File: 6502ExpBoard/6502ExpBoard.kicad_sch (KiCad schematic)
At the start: 5 parts, among them J1 Expansion / Diag Port, U1 74LS373, U2 74LS373, U3 74LS373, U4 74LS373

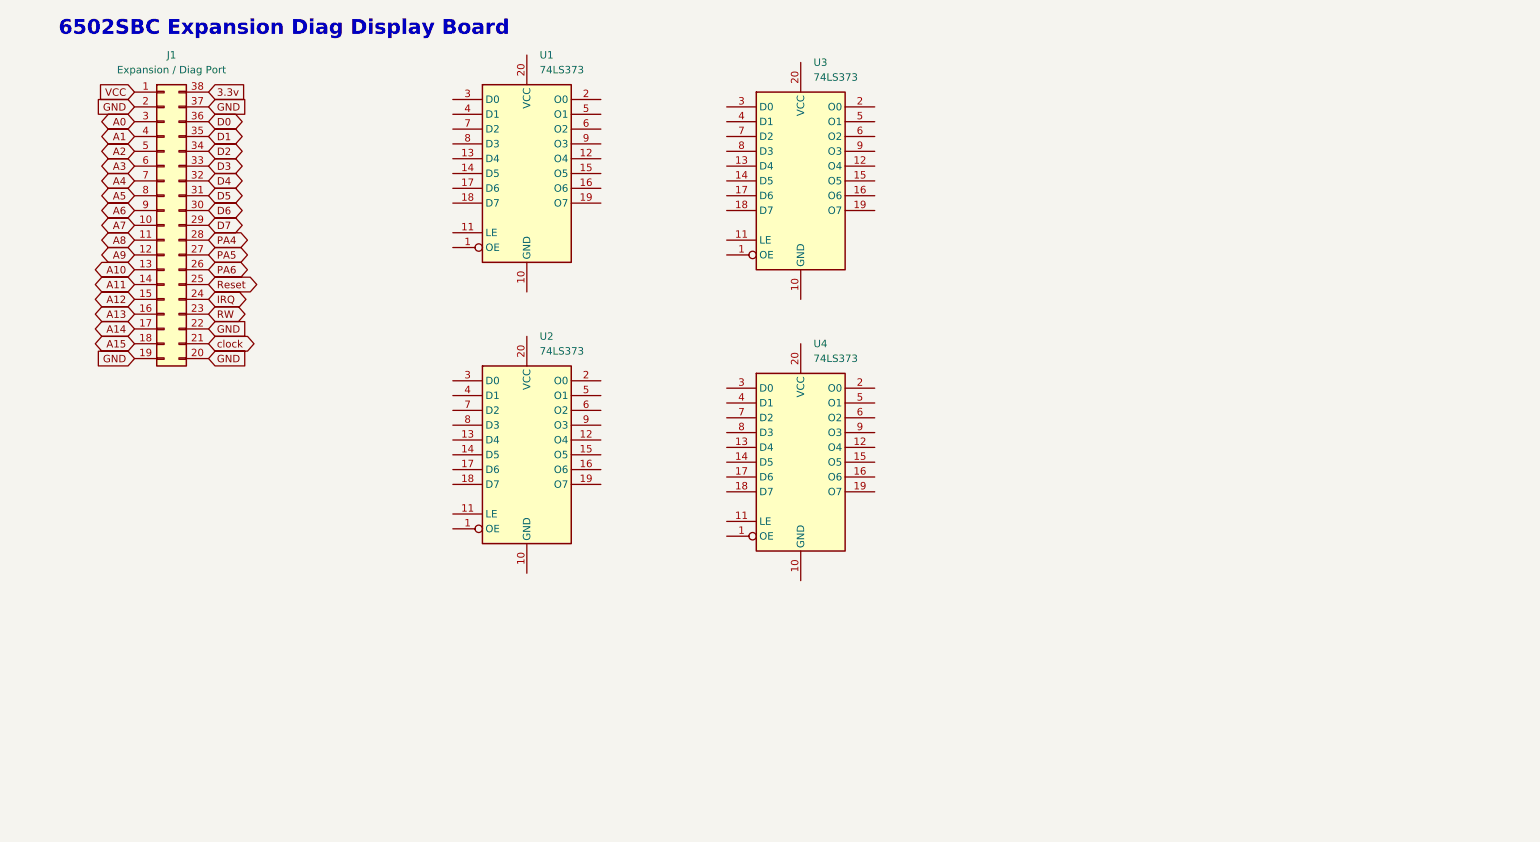
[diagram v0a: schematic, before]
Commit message: Added Expansion
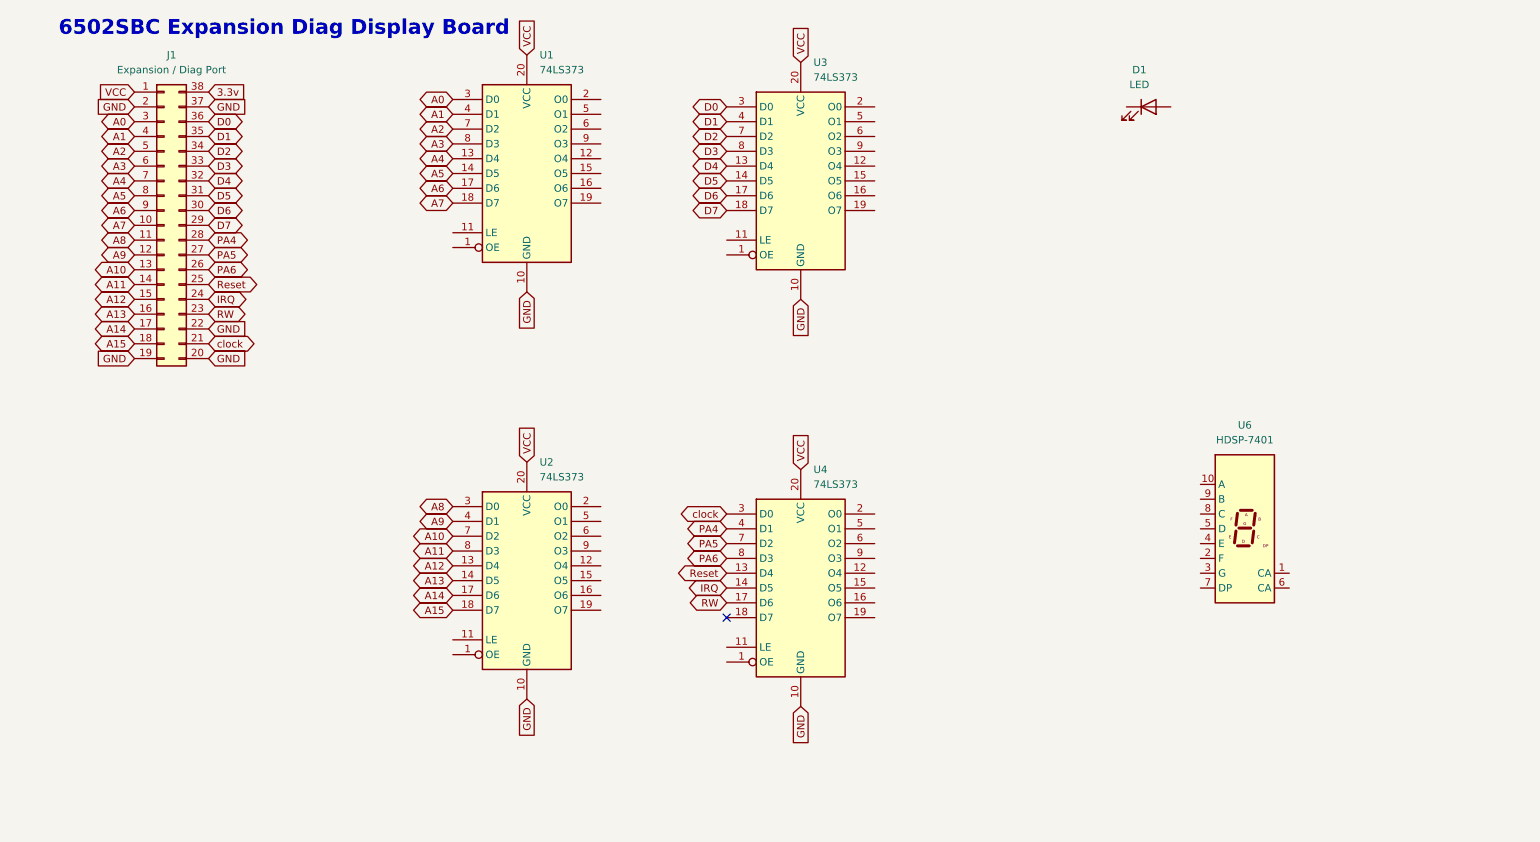
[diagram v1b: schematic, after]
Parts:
- added D1: LED, symbol Device:LED
- added U6: HDSP-7401, Display_7Segment:HDSP-7401, symbol Display_Character:HDSP-7401
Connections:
- net A0: now also U1.3 (D0)
- net A1: now also U1.4 (D1)
- net A10: now also U2.7 (D2)
- net A11: now also U2.8 (D3)
- net A12: now also U2.13 (D4)
- net A13: now also U2.14 (D5)
- net A14: now also U2.17 (D6)
- net A15: now also U2.18 (D7)
- net A2: now also U1.7 (D2)
- net A3: now also U1.8 (D3)
- net A4: now also U1.13 (D4)
- net A5: now also U1.14 (D5)
- net A6: now also U1.17 (D6)
- net A7: now also U1.18 (D7)
- net A8: now also U2.3 (D0)
- net A9: now also U2.4 (D1)
- net D0: now also U3.3 (D0)
- net D1: now also U3.4 (D1)
- net D2: now also U3.7 (D2)
- net D3: now also U3.8 (D3)
- net D4: now also U3.13 (D4)
- net D5: now also U3.14 (D5)
- net D6: now also U3.17 (D6)
- net D7: now also U3.18 (D7)
- net GND: now also U1.10 (GND), U2.10 (GND), U3.10 (GND), U4.10 (GND)
- net IRQ: now also U4.14 (D5)
- net PA4: now also U4.4 (D1)
- net PA5: now also U4.7 (D2)
- net PA6: now also U4.8 (D3)
- net RW: now also U4.17 (D6)
- net Reset: now also U4.13 (D4)
- net VCC: now also U1.20 (VCC), U2.20 (VCC), U3.20 (VCC), U4.20 (VCC)
- net clock: now also U4.3 (D0)
- no-connect marks 0 -> 1
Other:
- moved on the sheet: U2, U4

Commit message: Added Expansion
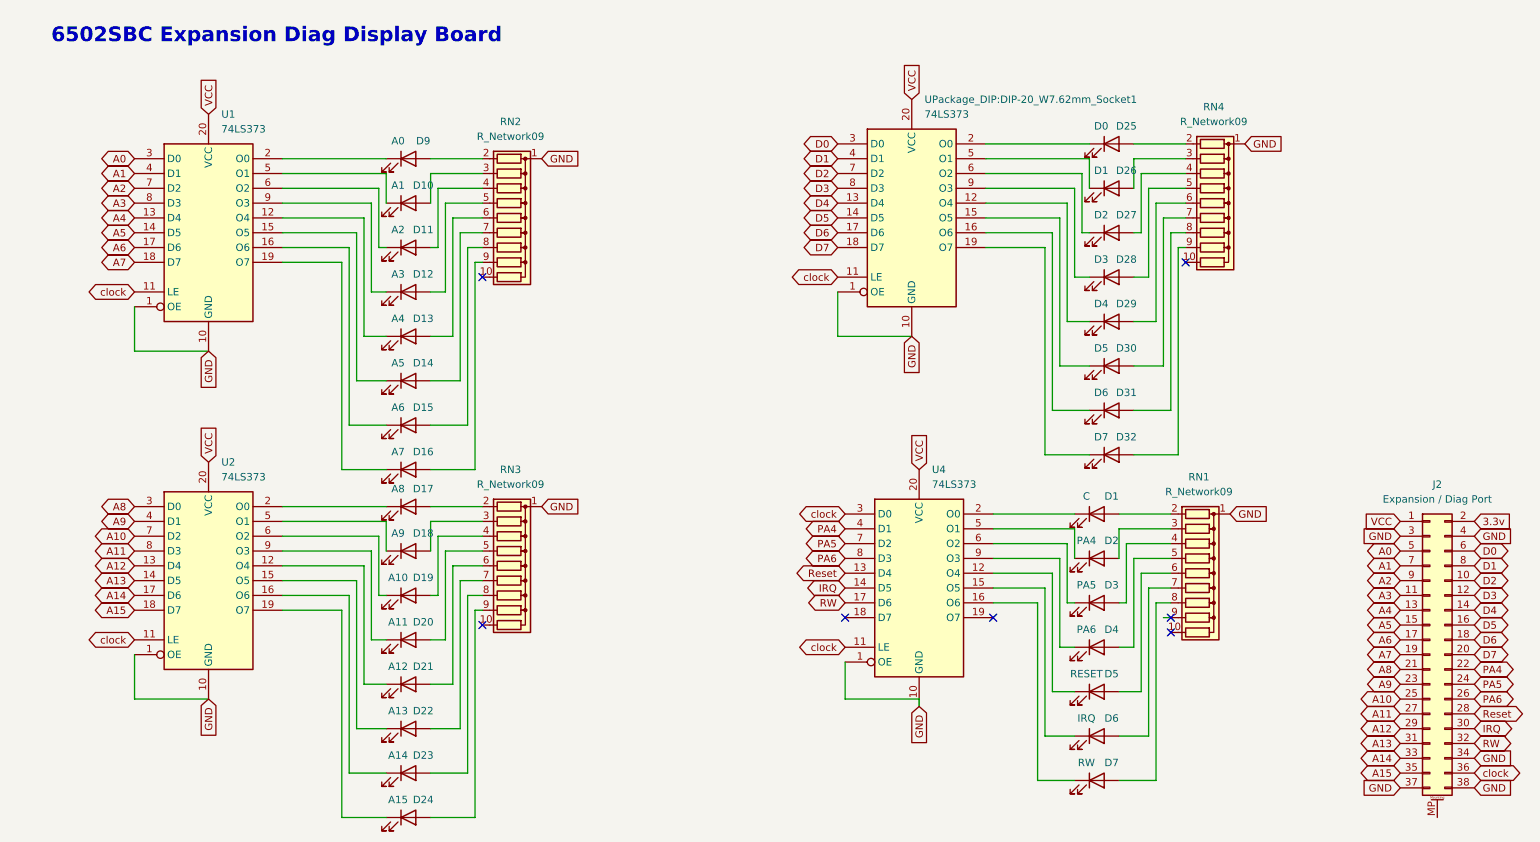
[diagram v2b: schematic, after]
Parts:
- removed J1: Expansion / Diag Port, Connector_PinHeader_2.54mm:PinHeader_1x38_P2.54mm_Horizontal, symbol Connector_Generic:Conn_02x19_Counter_Clockwise
- removed U6: HDSP-7401, Display_7Segment:HDSP-7401, symbol Display_Character:HDSP-7401
- added D10: A1, LED_THT:LED_D3.0mm, symbol Device:LED
- added D11: A2, LED_THT:LED_D3.0mm, symbol Device:LED
- added D12: A3, LED_THT:LED_D3.0mm, symbol Device:LED
- added D13: A4, LED_THT:LED_D3.0mm, symbol Device:LED
- added D14: A5, LED_THT:LED_D3.0mm, symbol Device:LED
- added D15: A6, LED_THT:LED_D3.0mm, symbol Device:LED
- added D16: A7, LED_THT:LED_D3.0mm, symbol Device:LED
- added D17: A8, LED_THT:LED_D3.0mm, symbol Device:LED
- added D18: A9, LED_THT:LED_D3.0mm, symbol Device:LED
- added D19: A10, LED_THT:LED_D3.0mm, symbol Device:LED
- added D2: PA4, LED_THT:LED_D3.0mm, symbol Device:LED
- added D20: A11, LED_THT:LED_D3.0mm, symbol Device:LED
- added D21: A12, LED_THT:LED_D3.0mm, symbol Device:LED
- added D22: A13, LED_THT:LED_D3.0mm, symbol Device:LED
- added D23: A14, LED_THT:LED_D3.0mm, symbol Device:LED
- added D24: A15, LED_THT:LED_D3.0mm, symbol Device:LED
- added D25: D0, LED_THT:LED_D3.0mm, symbol Device:LED
- added D26: D1, LED_THT:LED_D3.0mm, symbol Device:LED
- added D27: D2, LED_THT:LED_D3.0mm, symbol Device:LED
- added D28: D3, LED_THT:LED_D3.0mm, symbol Device:LED
- added D29: D4, LED_THT:LED_D3.0mm, symbol Device:LED
- added D3: PA5, LED_THT:LED_D3.0mm, symbol Device:LED
- added D30: D5, LED_THT:LED_D3.0mm, symbol Device:LED
- added D31: D6, LED_THT:LED_D3.0mm, symbol Device:LED
- added D32: D7, LED_THT:LED_D3.0mm, symbol Device:LED
- added D4: PA6, LED_THT:LED_D3.0mm, symbol Device:LED
- added D5: RESET, LED_THT:LED_D3.0mm, symbol Device:LED
- added D6: IRQ, LED_THT:LED_D3.0mm, symbol Device:LED
- added D7: RW, LED_THT:LED_D3.0mm, symbol Device:LED
- added D9: A0, LED_THT:LED_D3.0mm, symbol Device:LED
- added J2: Expansion / Diag Port, Connector_PinHeader_2.54mm:PinHeader_2x19_P2.54mm_Vertical, symbol Connector_Generic_MountingPin:Conn_02x19_Odd_Even_MountingPin
- added RN1, RN2, RN3, RN4: R_Network09, Resistor_THT:R_Array_SIP10, symbol Device:R_Network09
- D1: value LED -> C; footprint (none) -> LED_THT:LED_D3.0mm
- U1, U2, U4: footprint (none) -> Package_DIP:DIP-20_W7.62mm_Socket
- UPackage_DIP:DIP-20_W7.62mm_Socket1: renamed from U3; footprint (none) -> Package_DIP:DIP-20_W7.62mm_Socket
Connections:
- net 3.3v: now also J2.2 (Pin_2)
- net A0: now also J2.5 (Pin_5)
- net A1: now also J2.7 (Pin_7)
- net A10: now also J2.25 (Pin_25)
- net A11: now also J2.27 (Pin_27)
- net A12: now also J2.29 (Pin_29)
- net A13: now also J2.31 (Pin_31)
- net A14: now also J2.33 (Pin_33)
- net A15: now also J2.35 (Pin_35)
- net A2: now also J2.9 (Pin_9)
- net A3: now also J2.11 (Pin_11)
- net A4: now also J2.13 (Pin_13)
- net A5: now also J2.15 (Pin_15)
- net A6: now also J2.17 (Pin_17)
- net A7: now also J2.19 (Pin_19)
- net A8: now also J2.21 (Pin_21)
- net A9: now also J2.23 (Pin_23)
- net D0: now also J2.6 (Pin_6)
- net D1: now also J2.8 (Pin_8)
- net D2: now also J2.10 (Pin_10)
- net D3: now also J2.12 (Pin_12)
- net D4: now also J2.14 (Pin_14)
- net D5: now also J2.16 (Pin_16)
- net D6: now also J2.18 (Pin_18)
- net D7: now also J2.20 (Pin_20)
- net GND: now also U1.1 (OE), U2.1 (OE), U4.1 (OE), UPackage_DIP:DIP-20_W7.62mm_Socket1.1 (OE), J2.3 (Pin_3), J2.34 (Pin_34), J2.37 (Pin_37), J2.38 (Pin_38), J2.4 (Pin_4), RN1.1 (common), RN2.1 (common), RN3.1 (common), RN4.1 (common)
- net IRQ: now also J2.30 (Pin_30)
- net PA4: now also J2.22 (Pin_22)
- net PA5: now also J2.24 (Pin_24)
- net PA6: now also J2.26 (Pin_26)
- net RW: now also J2.32 (Pin_32)
- net Reset: now also J2.28 (Pin_28)
- net VCC: now also J2.1 (Pin_1)
- net clock: now also U1.11 (LE), U2.11 (LE), U4.11 (LE), UPackage_DIP:DIP-20_W7.62mm_Socket1.11 (LE), J2.36 (Pin_36)
- net at U4.12 (O4): now also D5.1 (K)
- net at U4.15 (O5): now also D6.1 (K)
- net at U4.16 (O6): now also D7.1 (K)
- net at U4.2 (O0): now also D1.1 (K)
- net at U4.5 (O1): now also D2.1 (K)
- net at U4.6 (O2): now also D3.1 (K)
- net at U4.9 (O3): now also D4.1 (K)
- net at D1.2 (A): now also RN1.2 (R1)
- net at UPackage_DIP:DIP-20_W7.62mm_Socket1.12 (O4): now also D29.1 (K)
- net at UPackage_DIP:DIP-20_W7.62mm_Socket1.15 (O5): now also D30.1 (K)
- net at UPackage_DIP:DIP-20_W7.62mm_Socket1.16 (O6): now also D31.1 (K)
- net at UPackage_DIP:DIP-20_W7.62mm_Socket1.19 (O7): now also D32.1 (K)
- net at UPackage_DIP:DIP-20_W7.62mm_Socket1.2 (O0): now also D25.1 (K)
- net at UPackage_DIP:DIP-20_W7.62mm_Socket1.5 (O1): now also D26.1 (K)
- net at UPackage_DIP:DIP-20_W7.62mm_Socket1.6 (O2): now also D27.1 (K)
- net at UPackage_DIP:DIP-20_W7.62mm_Socket1.9 (O3): now also D28.1 (K)
- net at U1.12 (O4): now also D13.1 (K)
- net at U1.15 (O5): now also D14.1 (K)
- net at U1.16 (O6): now also D15.1 (K)
- net at U1.19 (O7): now also D16.1 (K)
- net at U1.2 (O0): now also D9.1 (K)
- net at U1.5 (O1): now also D10.1 (K)
- net at U1.6 (O2): now also D11.1 (K)
- net at U1.9 (O3): now also D12.1 (K)
- net at U2.12 (O4): now also D21.1 (K)
- net at U2.15 (O5): now also D22.1 (K)
- net at U2.16 (O6): now also D23.1 (K)
- net at U2.19 (O7): now also D24.1 (K)
- net at U2.2 (O0): now also D17.1 (K)
- net at U2.5 (O1): now also D18.1 (K)
- net at U2.6 (O2): now also D19.1 (K)
- net at U2.9 (O3): now also D20.1 (K)
- new net: D18.2 (A), RN3.3 (R2)
- new net: D24.2 (A), RN3.9 (R8)
- new net: D6.2 (A), RN1.7 (R6)
- new net: D17.2 (A), RN3.2 (R1)
- new net: D19.2 (A), RN3.4 (R3)
- new net: D23.2 (A), RN3.8 (R7)
- new net: D27.2 (A), RN4.4 (R3)
- new net: D26.2 (A), RN4.3 (R2)
- new net: D14.2 (A), RN2.7 (R6)
- new net: D30.2 (A), RN4.7 (R6)
- new net: D31.2 (A), RN4.8 (R7)
- new net: D5.2 (A), RN1.6 (R5)
- new net: D20.2 (A), RN3.5 (R4)
- new net: D21.2 (A), RN3.6 (R5)
- new net: D22.2 (A), RN3.7 (R6)
- new net: D10.2 (A), RN2.3 (R2)
- new net: D11.2 (A), RN2.4 (R3)
- new net: D25.2 (A), RN4.2 (R1)
- new net: D28.2 (A), RN4.5 (R4)
- new net: D29.2 (A), RN4.6 (R5)
- new net: D32.2 (A), RN4.9 (R8)
- new net: D15.2 (A), RN2.8 (R7)
- new net: D2.2 (A), RN1.3 (R2)
- new net: D3.2 (A), RN1.4 (R3)
- new net: D4.2 (A), RN1.5 (R4)
- new net: D7.2 (A), RN1.8 (R7)
- new net: D16.2 (A), RN2.9 (R8)
- new net: D13.2 (A), RN2.6 (R5)
- new net: D9.2 (A), RN2.2 (R1)
- new net: D12.2 (A), RN2.5 (R4)
- no-connect marks 1 -> 7
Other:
- moved on the sheet: D1, U1, U2, U4, UPackage_DIP:DIP-20_W7.62mm_Socket1

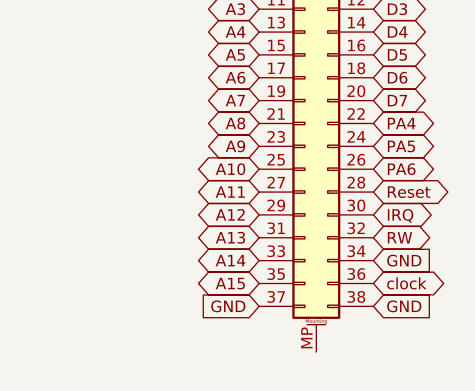
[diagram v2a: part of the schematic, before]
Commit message: Added Expansion
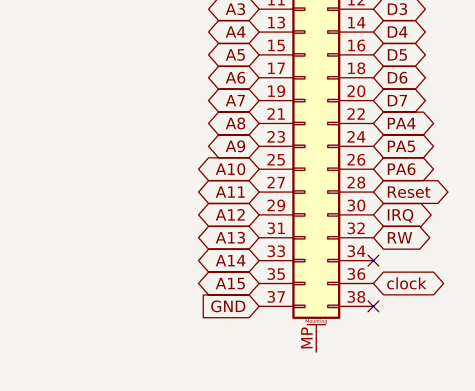
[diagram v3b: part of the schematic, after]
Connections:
- net GND: no longer J2.34 (Pin_34), J2.38 (Pin_38)
- no-connect marks 7 -> 9
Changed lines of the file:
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@@
+	)
+	(no_connect
+		(at 259.08 143.51)
+	)
+	(no_connect
+		(at 259.08 148.59)
 	)
 	(no_connect
@@
 		)
 	)
-	(global_label "GND"
-		(shape input)
-		(at 259.08 148.59 0)
-		(fields_autoplaced yes)
-		(effects
-			(font
-				(size 1.27 1.27)
-			)
-			(justify left)
-		)
-		(property "Intersheetrefs" "${INTERSHEET_REFS}"
-			(at 265.9357 148.59 0)
-			(effects
-				(font
-					(size 1.27 1.27)
-				)
-				(justify left)
-				(hide yes)
-			)
-		)
-	)
 	(global_label "D3"
 		(shape bidirectional)
@@
 				(hide yes)
 			)
-		)
-	)
-	(global_label "GND"
-		(shape input)
-		(at 259.08 143.51 0)
-		(fields_autoplaced yes)
-		(effects
-			(font
-				(size 1.27 1.27)
-			)
-			(justify left)
-		)
-		(property "Intersheetrefs" "${INTERSHEET_REFS}"
-			(at 265.9357 143.51 0)
-			(effects
-				(font
-					(size 1.27 1.27)
-				)
-				(justify left)
-				(hide yes)
-			)
